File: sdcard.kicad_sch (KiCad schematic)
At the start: 21 parts, among them J7 microSD push-pull, Q1 DMG2301L, Q2 2N7002, U3 SRV05-4, U4 SRV05-4

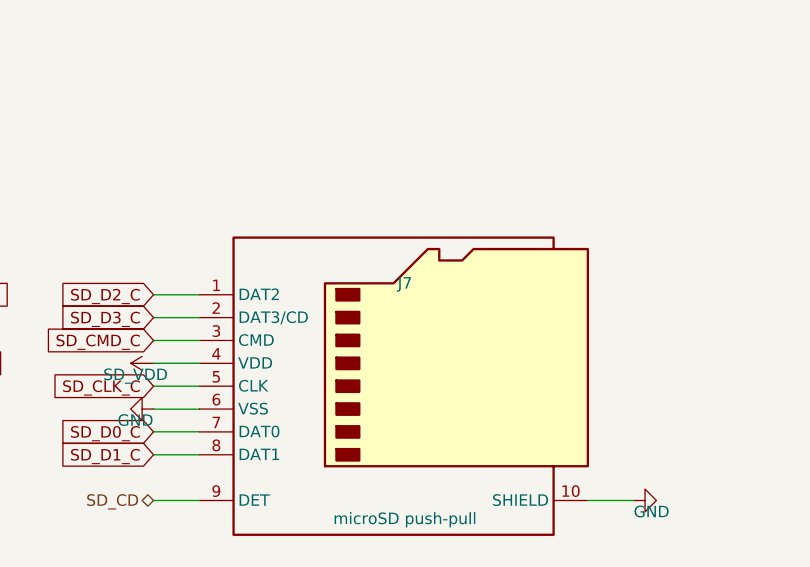
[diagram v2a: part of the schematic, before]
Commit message: Route, audit and document the carrier; verify every part number against the catalogue
Ordering is the point of this pass, so the part numbers came first. Every
LCSC number on the board was opened and read -- manufacturer part, package,
and the parameter that decides whether it is the right part. That found:

  C2148396 for the MCP2518FD    is an 18.7k resistor, out of stock -> C626759
  C255909  for a 40 MHz crystal is a 16 MHz crystal              -> C5186937
  C157966  for a JST PH 10-way  is a JST XH 9-way, 2.5 mm pitch  -> C158038

Three of the five numbers introduced last sitting were wrong, and all three
were plausible enough that the BOM exported clean. docs/PARTS.md records the
lot, including that LCSC's own listing for the microSD socket claims it has
no card-detect switch -- it has one, and the schematic is right.

Two footprints would not have soldered: both polyfuses are 1812 parts sitting
on a 1206 land, inherited from the parent board where nothing had ever
compared a part's package against its footprint. And the generic-passive
table was keyed on value alone, so the 1206 positions added last sitting
would have ordered 0805 parts -- right resistance, wrong footprint, every
board. It is keyed on (value, package) now and returns nothing rather than
guessing, so an unmatched line has no part number and somebody has to look.

Several values moved to match what is actually stocked: the power-fail
divider to 43k/18k (same trip point to 2 mV, both stocked 1 % parts), the
K-line series and pull-up to 20 R and 750 R, and the supercap charge resistor
from 22 R to 100 R -- 22 R put 1 W into a 250 mW part for the first several
seconds of every power-up.

Two real defects, both found by tools rather than by reading:

  - The hold-up Schottky was BACKWARDS. Reversed it shorts out the inrush
    limiter and blocks the discharge, so the supercap bank could never hold
    the rail up and the whole hold-up circuit was inert. audit_polarity found
    it once its expectat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
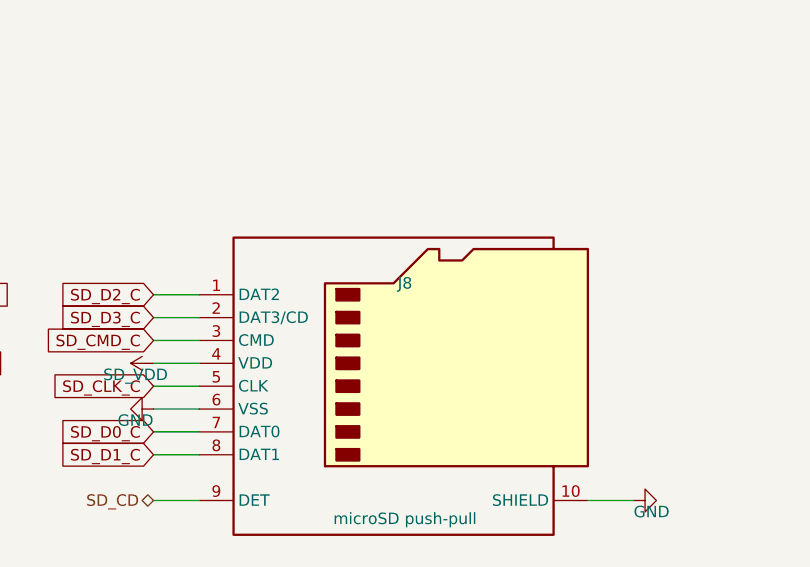
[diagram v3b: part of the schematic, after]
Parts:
- removed J7: microSD push-pull, Connector_Card:microSD_HC_Hirose_DM3D-SF, symbol Connector:Micro_SD_Card_Det1
- added J8: microSD push-pull, Connector_Card:microSD_HC_Hirose_DM3D-SF, symbol Connector:Micro_SD_Card_Det1
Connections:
- net GND: now also J8.10 (SHIELD), J8.6 (VSS)
- net SD_CD: now also J8.9 (DET)
- net SD_CLK_C: now also J8.5 (CLK)
- net SD_CMD_C: now also J8.3 (CMD)
- net SD_D0_C: now also J8.7 (DAT0)
- net SD_D1_C: now also J8.8 (DAT1)
- net SD_D2_C: now also J8.1 (DAT2)
- net SD_D3_C: now also J8.2 (DAT3/CD)
- net SD_VDD: now also J8.4 (VDD)
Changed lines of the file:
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@@
   (symbol (lib_id "Connector:Micro_SD_Card_Det1") (at 135.89 105.41 0) (unit 1)
     (in_bom yes) (on_board yes) (dnp no)
-    (property "Reference" "J7" (at 135.89 93.98 0)
+    (property "Reference" "J8" (at 135.89 93.98 0)
       (effects (font (size 1.27 1.27)) )
     )
@@
     (instances
       (project "esp32s3-can-sd-logger"
-        (path "/3276c6e6-7085-5954-8442-c6cef7eab316/229b8fda-064c-5815-a4c6-b9c2bb7e623c" (reference "J7") (unit 1))
+        (path "/3276c6e6-7085-5954-8442-c6cef7eab316/229b8fda-064c-5815-a4c6-b9c2bb7e623c" (reference "J8") (unit 1))
       )
     )

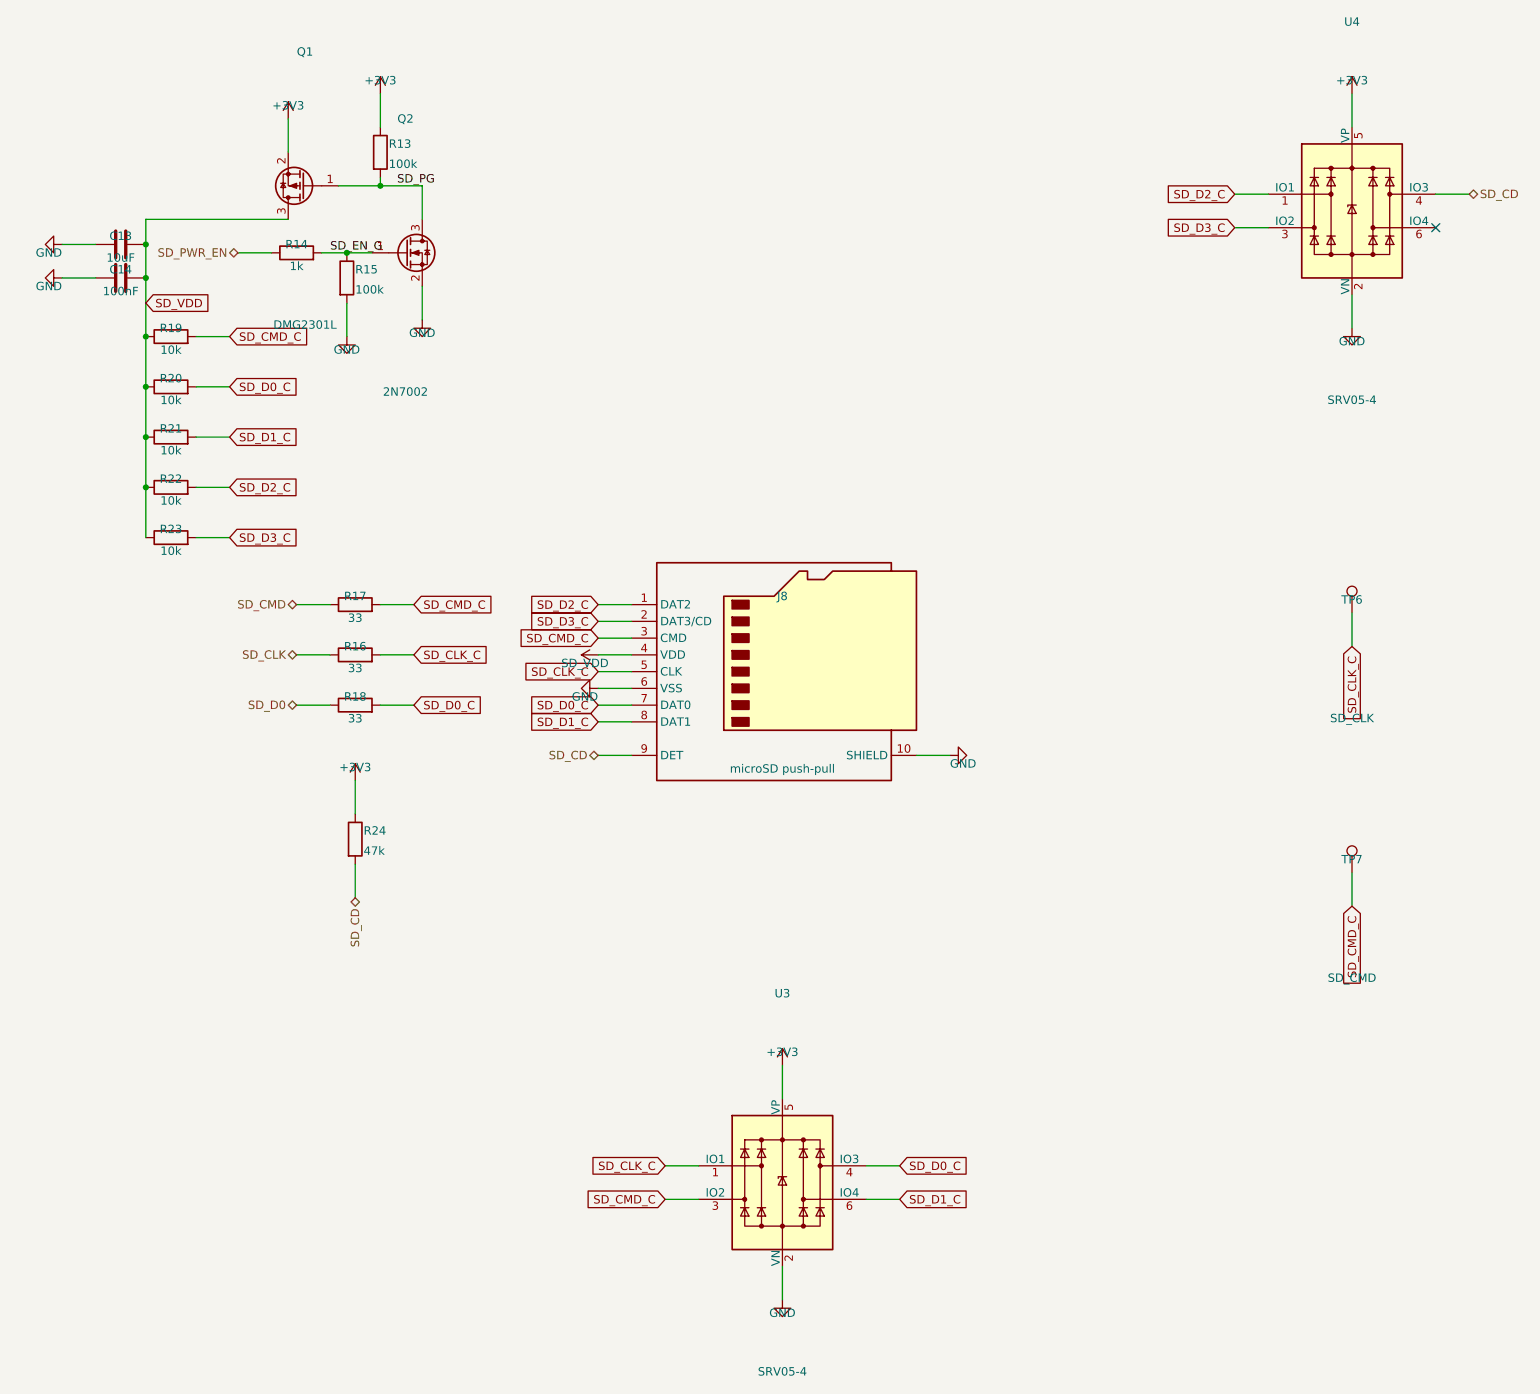
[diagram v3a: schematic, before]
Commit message: Make the schematic readable: wire the loose parts, stop text printing through symbols
Three things the drawing was doing badly, all now measured by a new
gen/audit_schematic.py rather than judged by eye.

LOOSE PARTS ARE WIRED NOW. A decoupling capacitor is a two-pin part with a
rail on each pin, and the column packer had no reason to put one next to
another -- so each came out as its own island with a net label at both ends,
twenty-odd of them down the edge of the power sheet. Electrically perfect,
visually a parts bin. build_ladders() groups the leftovers by which pair of
nets they sit across and draws each group as a proper ladder: one wire along
the top pins, one along the bottom, a junction at every rung and a power
symbol at each end. Nine groups across five sheets, including the supercap
bank and the battery monitor, and it removes two labels per part.

Grouping is on the actual pin GEOMETRY, not the symbol name, which is what
lets a balancing resistor share a ladder with the capacitor it balances while
keeping out a TVS diode whose pins are 1.3 mm closer together -- that one ERC
caught as two unconnected wire endpoints.

TEXT NO LONGER PRINTS THROUGH SYMBOLS. The offsets that place a reference and
a value work from the box around a part's PINS, and a symbol's graphic is
routinely drawn outside it. A power symbol's arrow therefore went straight
through its own name -- "+5VS" read "+2VS" at a glance, which is exactly how
somebody ends up probing the wrong rail -- and a capacitor lying on its side
has a y extent of exactly zero, so its reference and value printed across the
plates. Both now work from a floor on the body size. Rail names are also
centred on their own pin instead of drooping half a pitch onto the next one,
and the solder jumpers lost "(default OFF)" from their value into their note,
which is eighteen characters of text on a part 1.3 mm wide.

THE HAND-DRAWN BLOCKS WERE RE-SPACED to suit, because their tables were laid
out when the text sat closer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
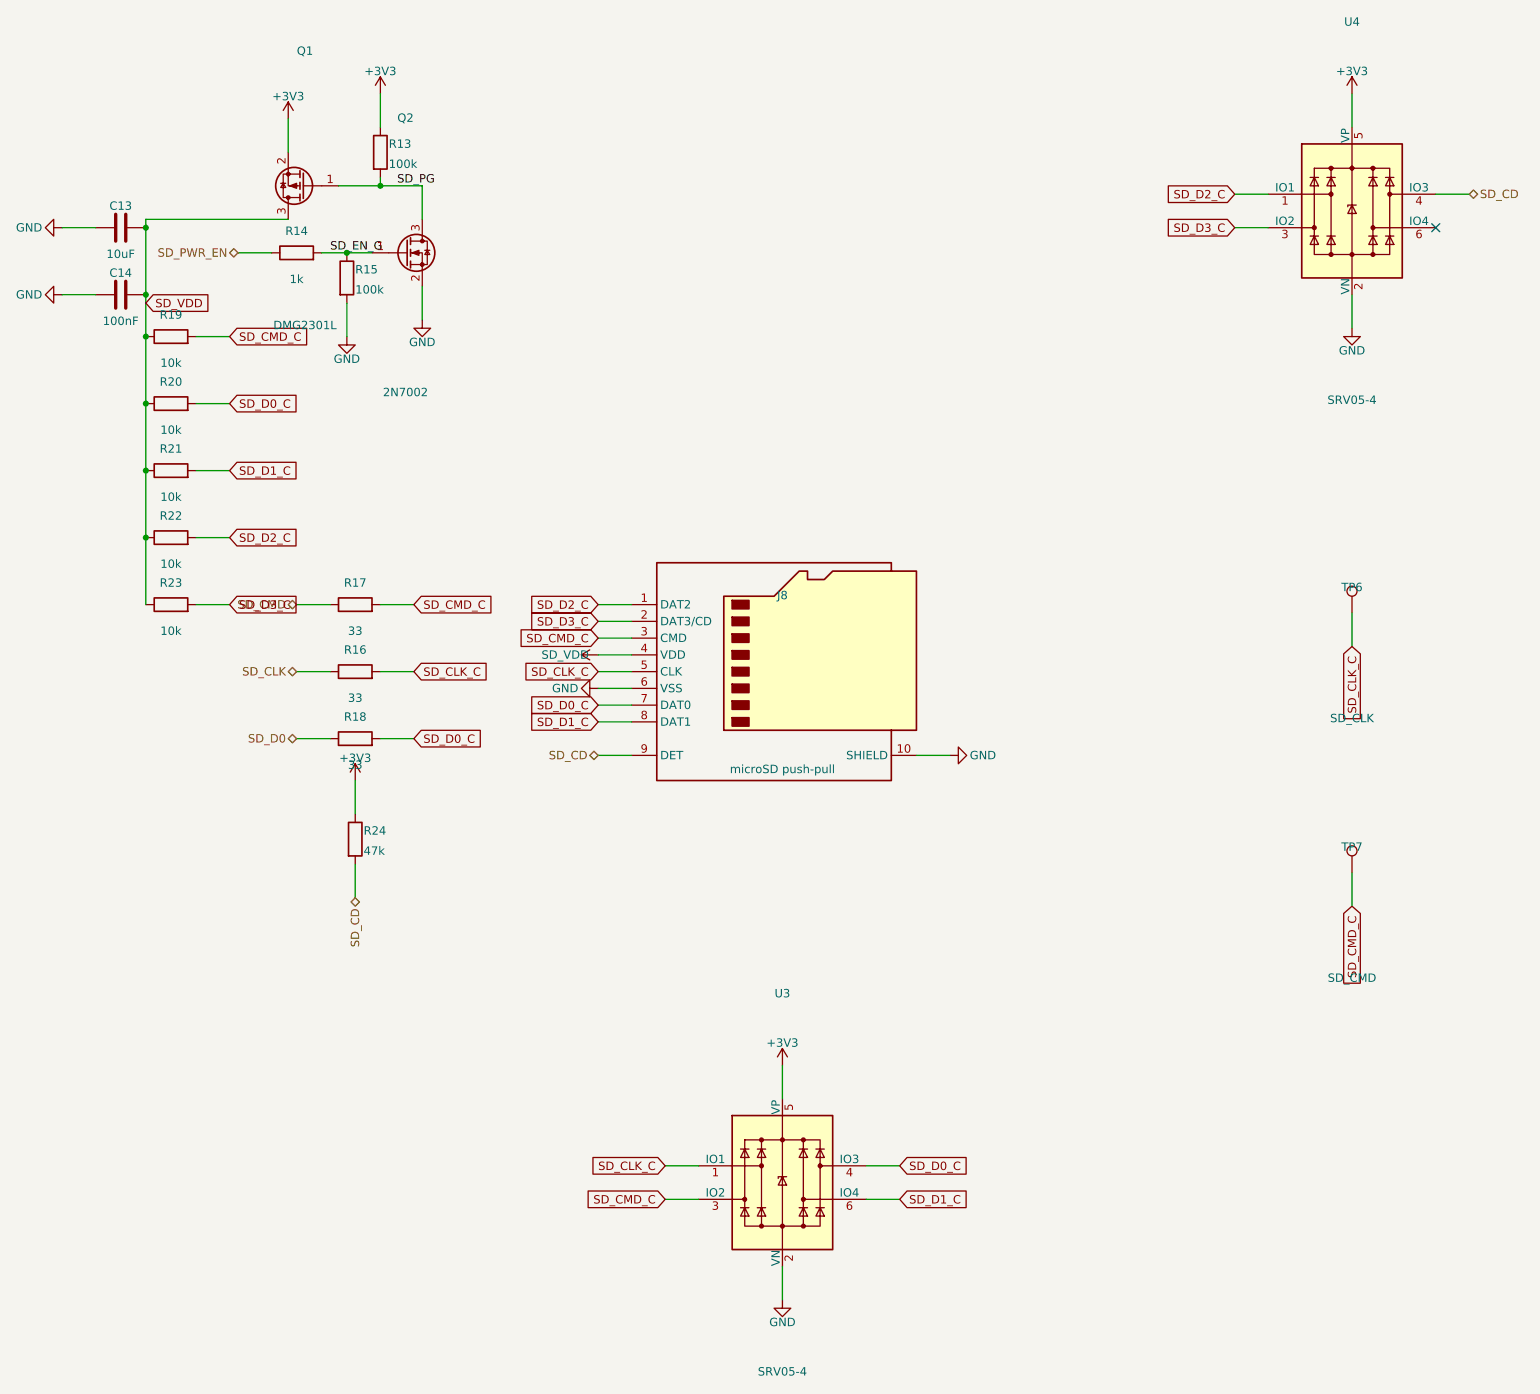
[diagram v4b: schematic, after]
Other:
- moved on the sheet: C13, C14, R16, R18, R20, R21, R22, R23
